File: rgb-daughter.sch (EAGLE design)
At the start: 11 parts, among them J1 INPUT

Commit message: feat(planck): add caps
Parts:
- added C10, C11, C12, C13, C15, C16, C17, C18, C19, C2, C20, C21, C22, C23, C24, C25, C26, C27, C28, C29, C3, C30, C31, C32, C33, C34, C35, C36, C37, C38, C39, C4, C40, C41, C42, C43, C44, C45, C46, C47, C48, C5, C6, C7, C8, C9: 0.1uF, SparkFun-Capacitors:0.1UF-0603-25V-(+80/-20%)
- added FRAME2: FRAME-LETTER, SparkFun-Aesthetics:FRAME-LETTER
- added LED10, LED11, LED12, LED13, LED14, LED15, LED16, LED17, LED18, LED19, LED20, LED21, LED22, LED23, LED24, LED25, LED26, LED27, LED28, LED29, LED30, LED31, LED32, LED33, LED34, LED35, LED36, LED37, LED38, LED39, LED40, LED41, LED42, LED43, LED44, LED45, LED46, LED47, LED7, LED8, LED9: WS2812B5050, adafruit:WS2812B5050
- C1: value 100uF -> 0.1uF; device capacitor-wima:C2,5-3 -> SparkFun-Capacitors:0.1UF-0603-25V-(+80/-20%)
- J1: device SparkFun-Connectors:CONN_05 -> SparkFun-Connectors:CONN_051.27MM
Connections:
- new net DO: LED23.DO, LED25.DI
- new net N$10: LED8.DO, LED9.DI
- new net N$11: LED10.DI, LED9.DO
- new net N$12: LED10.DO, LED11.DI
- new net N$13: LED11.DO, LED12.DI
- new net N$14: LED14.DO, LED15.DI
- new net N$15: LED15.DO, LED16.DI
- new net N$16: LED16.DO, LED17.DI
- new net N$17: LED17.DO, LED18.DI
- new net N$18: LED19.DO, LED20.DI
- new net N$19: LED20.DO, LED21.DI
- new net N$20: LED21.DO, LED22.DI
- new net N$21: LED22.DO, LED23.DI
- new net N$22: LED24.DI, LED47.DO
- new net N$23: LED6.DO, LED7.DI
- new net N$24: LED13.DO, LED14.DI
- new net N$25: LED18.DO, LED19.DI
- new net N$26: LED25.DO, LED26.DI
- new net N$29: LED26.DO, LED27.DI
- new net N$30: LED27.DO, LED28.DI
- new net N$31: LED28.DO, LED29.DI
- new net N$32: LED29.DO, LED30.DI
- new net N$33: LED31.DO, LED32.DI
- new net N$34: LED32.DO, LED33.DI
- new net N$35: LED33.DO, LED34.DI
- new net N$36: LED34.DO, LED35.DI
- new net N$37: LED35.DO, LED36.DI
- new net N$38: LED38.DO, LED39.DI
- new net N$39: LED39.DO, LED40.DI
- new net N$40: LED40.DO, LED41.DI
- new net N$41: LED41.DO, LED42.DI
- new net N$42: LED43.DO, LED44.DI
- new net N$43: LED45.DO, LED46.DI
- new net N$44: LED46.DO, LED47.DI
- new net N$46: LED30.DO, LED31.DI
- new net N$47: LED36.DO, LED37.DI
- new net N$48: LED37.DO, LED38.DI
- new net N$49: LED42.DO, LED43.DI
- new net N$50: LED44.DO, LED45.DI
- new net N$8: LED7.DO, LED8.DI
- new net N$9: LED12.DO, LED13.DI
- net GND: now also C10.2, C11.2, C12.2, C13.2, C15.2, C16.2, C17.2, C18.2, C19.2, C2.2, C20.2, C21.2, C22.2, C23.2, C24.2, C25.2, C26.2, C27.2, C28.2, C29.2, C3.2, C30.2, C31.2, C32.2, C33.2, C34.2, C35.2, C36.2, C37.2, C38.2, C39.2, C4.2, C40.2, C41.2, C42.2, C43.2, C44.2, C45.2, C46.2, C47.2, C48.2, C5.2, C6.2, C7.2, C8.2, C9.2, LED10.GND, LED11.GND, LED12.GND, LED13.GND, LED14.GND, LED15.GND, LED16.GND, LED17.GND, LED18.GND, LED19.GND, LED20.GND, LED21.GND, LED22.GND, LED23.GND, LED24.GND, LED25.GND, LED26.GND, LED27.GND, LED28.GND, LED29.GND, LED30.GND, LED31.GND, LED32.GND, LED33.GND, LED34.GND, LED35.GND, LED36.GND, LED37.GND, LED38.GND, LED39.GND, LED40.GND, LED41.GND, LED42.GND, LED43.GND, LED44.GND, LED45.GND, LED46.GND, LED47.GND, LED7.GND, LED8.GND, LED9.GND
- net VDD: now also C10.1, C11.1, C12.1, C13.1, C15.1, C16.1, C17.1, C18.1, C19.1, C2.1, C20.1, C21.1, C22.1, C23.1, C24.1, C25.1, C26.1, C27.1, C28.1, C29.1, C3.1, C30.1, C31.1, C32.1, C33.1, C34.1, C35.1, C36.1, C37.1, C38.1, C39.1, C4.1, C40.1, C41.1, C42.1, C43.1, C44.1, C45.1, C46.1, C47.1, C48.1, C5.1, C6.1, C7.1, C8.1, C9.1, LED10.VDD, LED11.VDD, LED12.VDD, LED13.VDD, LED14.VDD, LED15.VDD, LED16.VDD, LED17.VDD, LED18.VDD, LED19.VDD, LED20.VDD, LED21.VDD, LED22.VDD, LED23.VDD, LED24.VDD, LED25.VDD, LED26.VDD, LED27.VDD, LED28.VDD, LED29.VDD, LED30.VDD, LED31.VDD, LED32.VDD, LED33.VDD, LED34.VDD, LED35.VDD, LED36.VDD, LED37.VDD, LED38.VDD, LED39.VDD, LED40.VDD, LED41.VDD, LED42.VDD, LED43.VDD, LED44.VDD, LED45.VDD, LED46.VDD, LED47.VDD, LED7.VDD, LED8.VDD, LED9.VDD

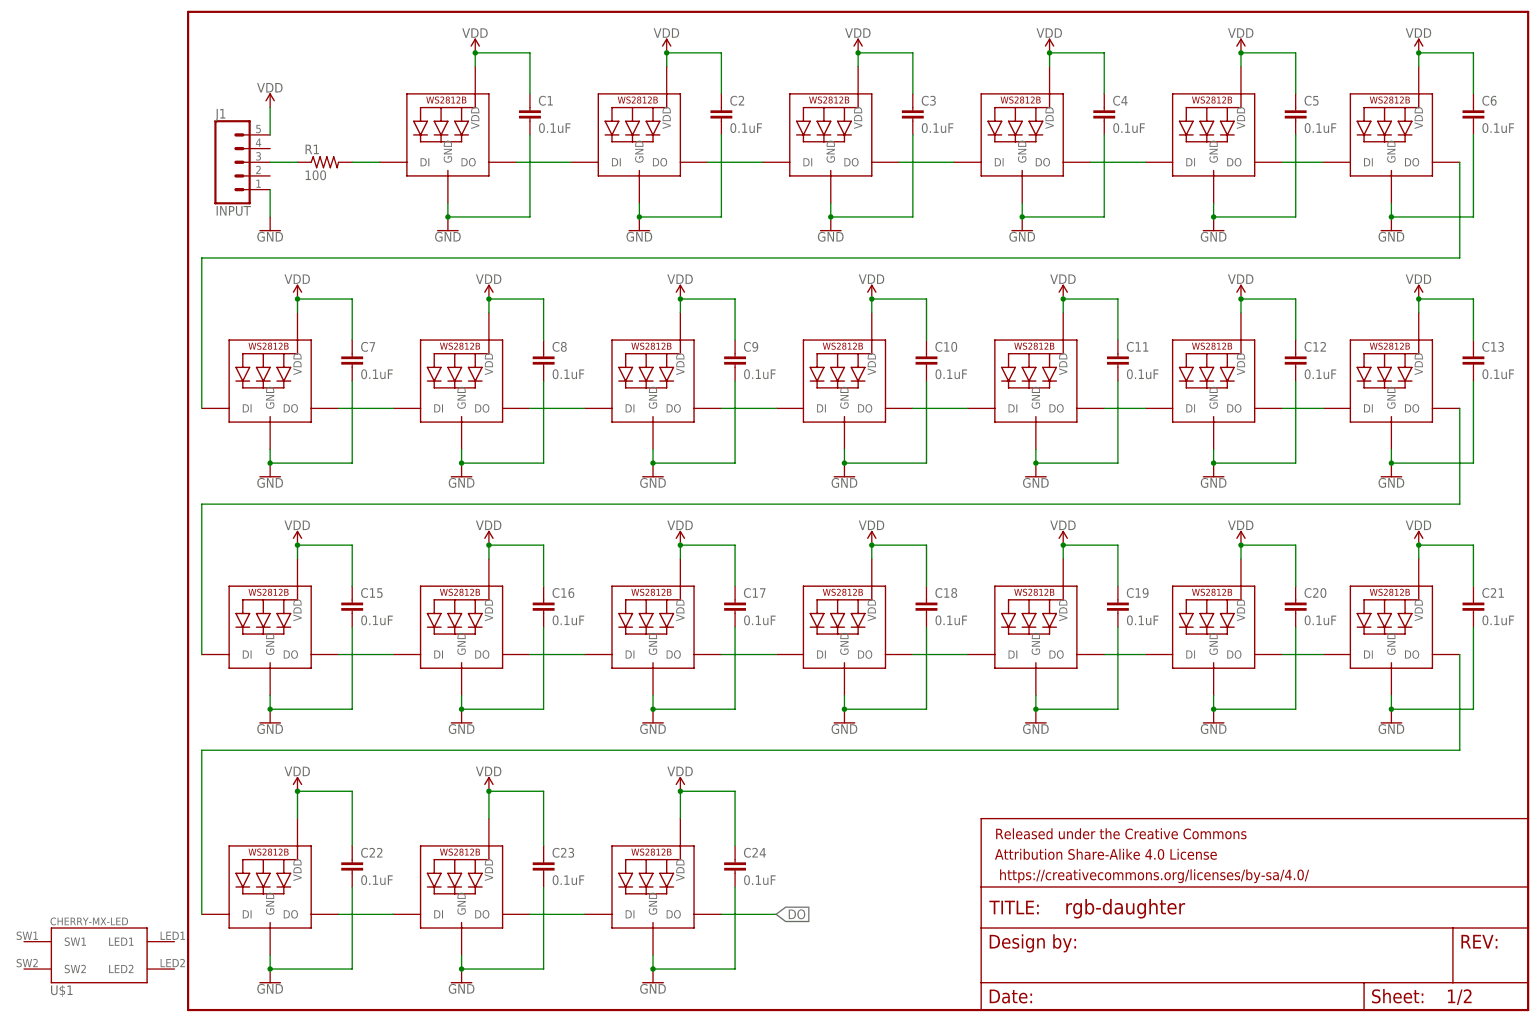
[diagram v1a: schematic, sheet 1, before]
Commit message: 🐛 rebuilding schematic with design blocks
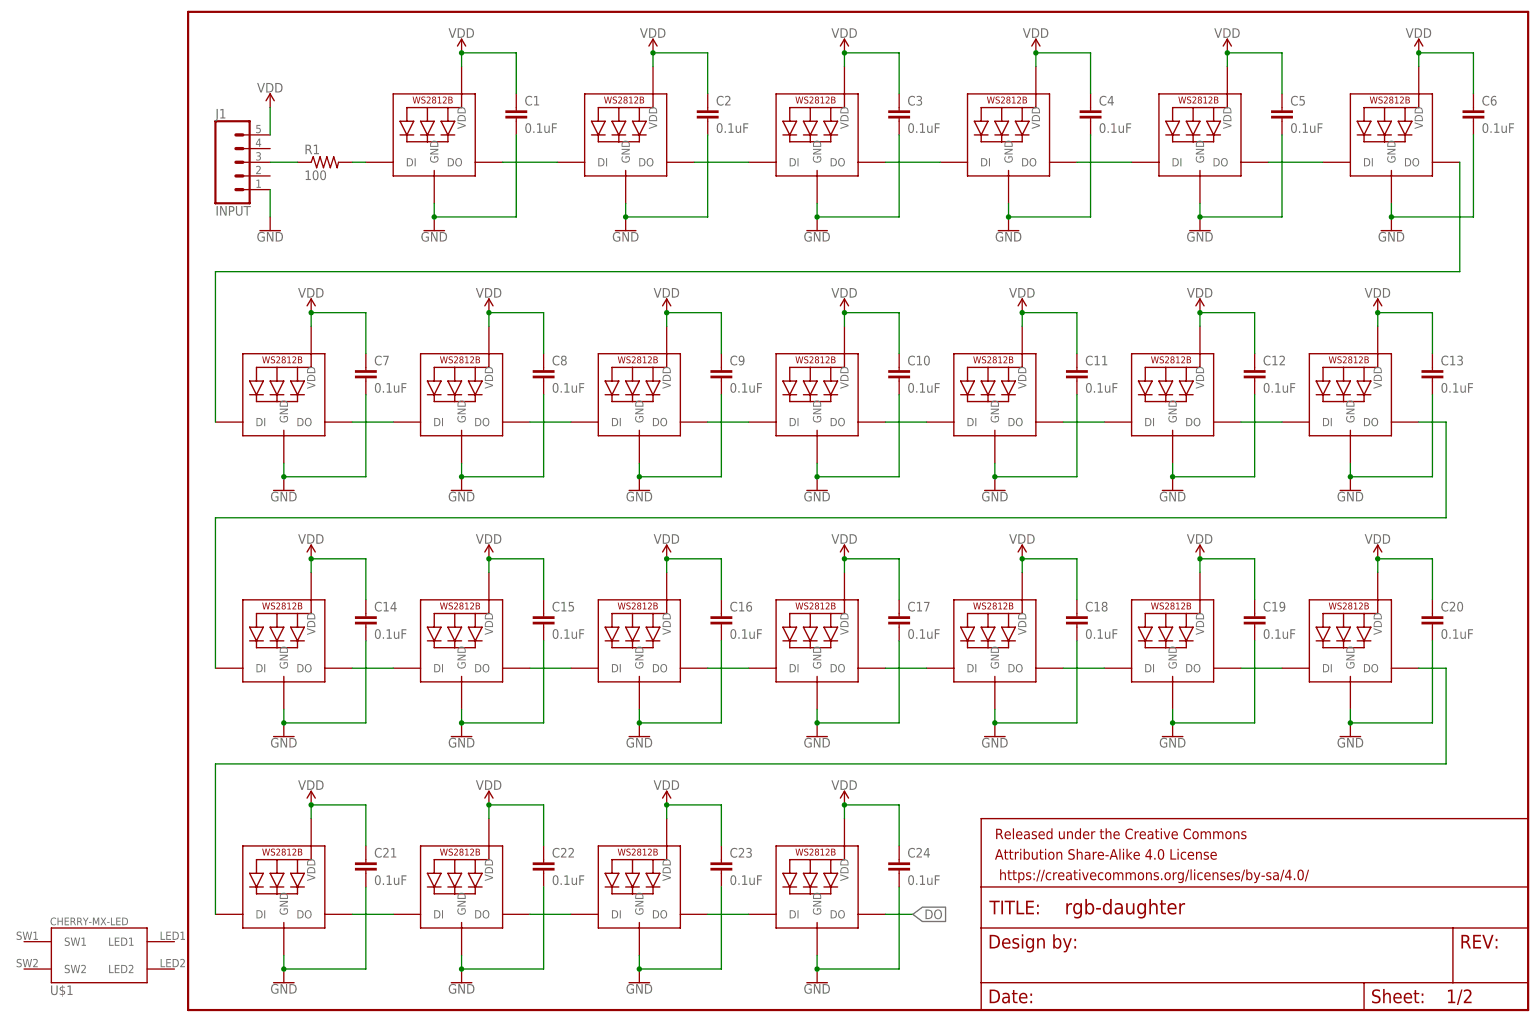
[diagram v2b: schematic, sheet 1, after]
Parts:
- added C14: 0.1uF, SparkFun-Capacitors:0.1UF-0603-25V-(+80/-20%)
- added LED48: WS2812B5050, adafruit:WS2812B5050
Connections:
- new net N$25: LED23.DO, LED48.DI
- net DO: now also LED24.DI, LED48.DO; no longer LED23.DO, LED25.DI
- net GND: now also C14.2, LED48.GND
- net N$22: now also LED24.DO, LED25.DI; no longer LED24.DI, LED47.DO
- net VDD: now also C14.1, LED48.VDD
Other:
- moved on the sheet: C1, C10, C11, C12, C13, C15, C16, C17, C18, C19, C2, C20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

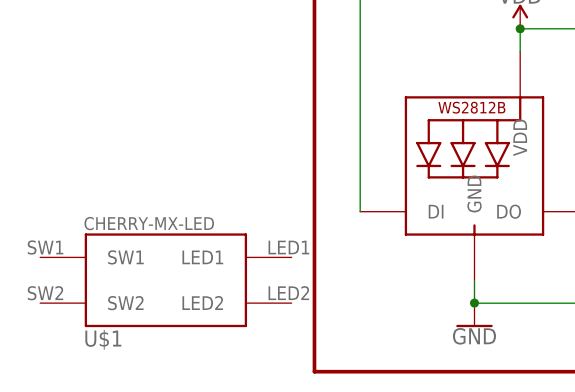
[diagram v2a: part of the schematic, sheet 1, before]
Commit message: 🔥 removing test cherry switch
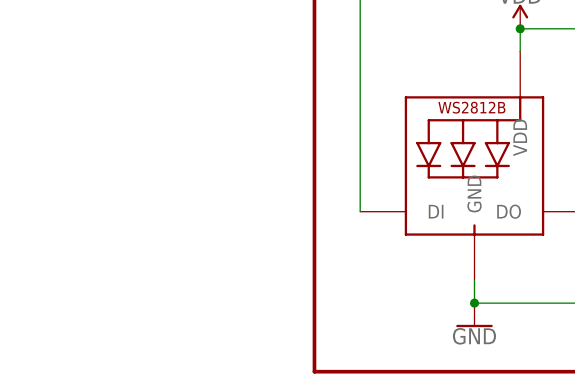
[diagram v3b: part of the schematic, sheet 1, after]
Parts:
- removed U$1: CHERRY-MX-LED, cherrymx:CHERRY-MX-LED
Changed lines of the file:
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@@
 <part name="SUPPLY1" library="SparkFun-PowerSymbols" library_urn="urn:adsk.eagle:library:530" deviceset="VDD" device=""/>
 <part name="R1" library="resistor" library_urn="urn:adsk.eagle:library:348" deviceset="R-US_" device="M0805" package3d_urn="urn:adsk.eagle:package:26079/1" value="100"/>
-<part name="U$1" library="cherrymx" deviceset="CHERRY-MX-LED" device=""/>
 <part name="FRAME2" library="SparkFun-Aesthetics" library_urn="urn:adsk.eagle:library:507" deviceset="FRAME-LETTER" device="" package3d_urn="urn:adsk.eagle:package:37121/1"/>
 <part name="LED1" library="adafruit" library_urn="urn:adsk.eagle:library:420" deviceset="WS2812B" device="5050"/>
@@
 <instance part="SUPPLY1" gate="VDD" x="15.24" y="167.64"/>
 <instance part="R1" gate="G$1" x="25.4" y="157.48"/>
-<instance part="U$1" gate="G$1" x="-20.32" y="10.16"/>
 <instance part="LED1" gate="G$1" x="45.72" y="160.02"/>
 <instance part="C1" gate="G$1" x="60.96" y="165.1"/>

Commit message: ⏪ Revert "🔥 removing test cherry switch"
This reverts commit f0bcf8e92973c98fa4b33c8b3d8bb0c59f9eaaca.
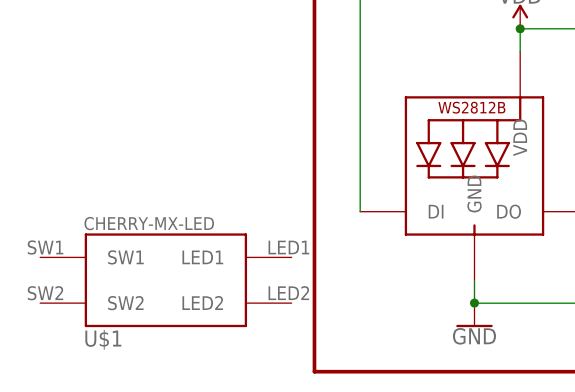
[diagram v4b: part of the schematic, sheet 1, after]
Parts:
- added U$1: CHERRY-MX-LED, cherrymx:CHERRY-MX-LED
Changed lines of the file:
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@@
 <part name="SUPPLY1" library="SparkFun-PowerSymbols" library_urn="urn:adsk.eagle:library:530" deviceset="VDD" device=""/>
 <part name="R1" library="resistor" library_urn="urn:adsk.eagle:library:348" deviceset="R-US_" device="M0805" package3d_urn="urn:adsk.eagle:package:26079/1" value="100"/>
+<part name="U$1" library="cherrymx" deviceset="CHERRY-MX-LED" device=""/>
 <part name="FRAME2" library="SparkFun-Aesthetics" library_urn="urn:adsk.eagle:library:507" deviceset="FRAME-LETTER" device="" package3d_urn="urn:adsk.eagle:package:37121/1"/>
 <part name="LED1" library="adafruit" library_urn="urn:adsk.eagle:library:420" deviceset="WS2812B" device="5050"/>
@@
 <instance part="SUPPLY1" gate="VDD" x="15.24" y="167.64"/>
 <instance part="R1" gate="G$1" x="25.4" y="157.48"/>
+<instance part="U$1" gate="G$1" x="-20.32" y="10.16"/>
 <instance part="LED1" gate="G$1" x="45.72" y="160.02"/>
 <instance part="C1" gate="G$1" x="60.96" y="165.1"/>

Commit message: 🚧📦 using ws2812b 3535
routes are currently screwed up
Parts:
- LED1, LED10, LED11, LED12, LED13, LED14, LED15, LED16, LED17, LED18, LED19, LED2, LED20, LED21, LED22, LED23, LED24, LED25, LED26, LED27, LED28, LED29, LED3, LED30, LED31, LED32, LED33, LED34, LED35, LED36, LED37, LED38, LED39, LED4, LED40, LED41, LED42, LED43, LED44, LED45, LED46, LED47, LED48, LED5, LED6, LED7, LED8, LED9: value WS2812B5050 -> WS2812B3535; device adafruit:WS2812B5050 -> adafruit:WS2812B3535

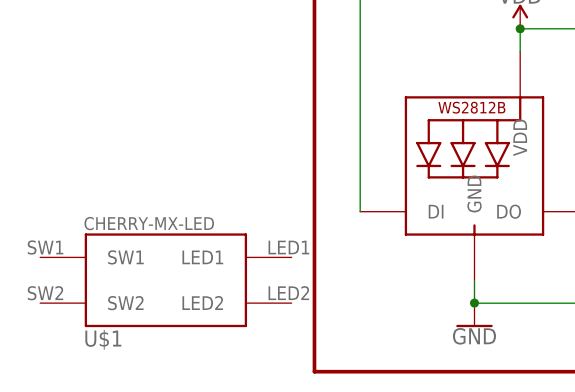
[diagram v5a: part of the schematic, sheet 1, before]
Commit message: 🔥 removing test cherry switch
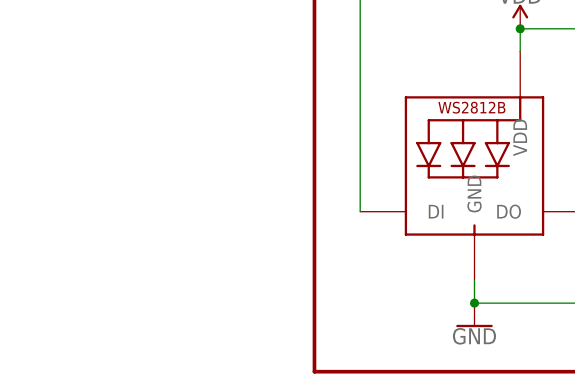
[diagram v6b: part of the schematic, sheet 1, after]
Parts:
- removed U$1: CHERRY-MX-LED, cherrymx:CHERRY-MX-LED
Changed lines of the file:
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@@
 <part name="SUPPLY1" library="SparkFun-PowerSymbols" library_urn="urn:adsk.eagle:library:530" deviceset="VDD" device=""/>
 <part name="R1" library="resistor" library_urn="urn:adsk.eagle:library:348" deviceset="R-US_" device="M0805" package3d_urn="urn:adsk.eagle:package:26079/1" value="100"/>
-<part name="U$1" library="cherrymx" deviceset="CHERRY-MX-LED" device=""/>
 <part name="FRAME2" library="SparkFun-Aesthetics" library_urn="urn:adsk.eagle:library:507" deviceset="FRAME-LETTER" device="" package3d_urn="urn:adsk.eagle:package:37121/1"/>
 <part name="LED1" library="adafruit" library_urn="urn:adsk.eagle:library:420" deviceset="WS2812B" device="3535" value="WS2812B3535"/>
@@
 <instance part="SUPPLY1" gate="VDD" x="15.24" y="167.64"/>
 <instance part="R1" gate="G$1" x="25.4" y="157.48"/>
-<instance part="U$1" gate="G$1" x="-20.32" y="10.16"/>
 <instance part="LED1" gate="G$1" x="45.72" y="160.02"/>
 <instance part="C1" gate="G$1" x="60.96" y="165.1"/>

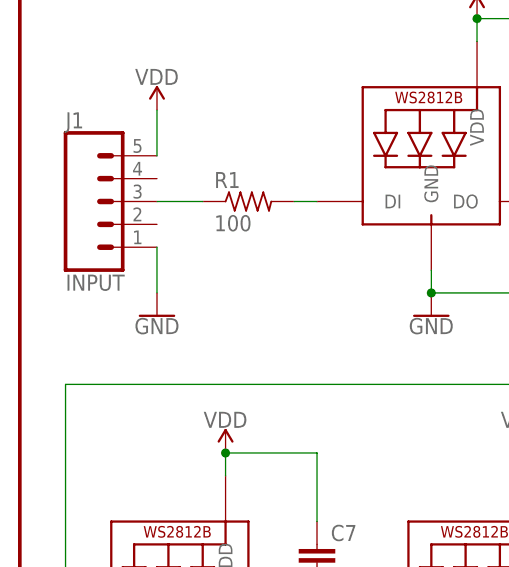
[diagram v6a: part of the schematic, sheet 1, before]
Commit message: 💄 converting text labels to attributes
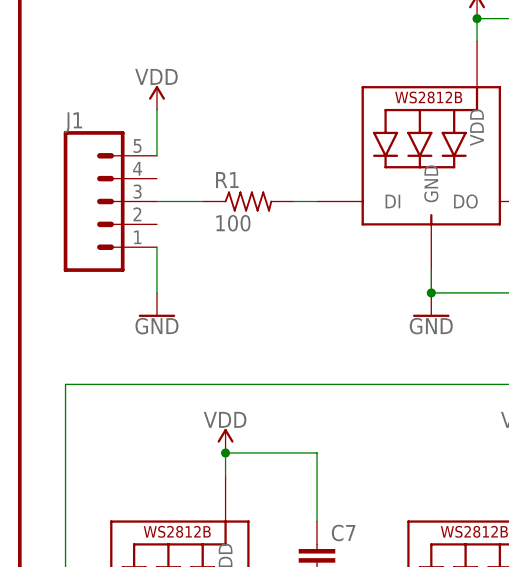
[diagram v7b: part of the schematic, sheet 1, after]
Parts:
- J1: value INPUT -> (none)
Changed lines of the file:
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@@
 <part name="FRAME1" library="SparkFun-Aesthetics" library_urn="urn:adsk.eagle:library:507" deviceset="FRAME-LETTER" device="" package3d_urn="urn:adsk.eagle:package:37121/1"/>
 <part name="GND1" library="SparkFun-PowerSymbols" library_urn="urn:adsk.eagle:library:530" deviceset="GND" device=""/>
-<part name="J1" library="SparkFun-Connectors" library_urn="urn:adsk.eagle:library:513" deviceset="CONN_05" device="1.27MM" package3d_urn="urn:adsk.eagle:package:38110/1" value="INPUT"/>
+<part name="J1" library="SparkFun-Connectors" library_urn="urn:adsk.eagle:library:513" deviceset="CONN_05" device="1.27MM" package3d_urn="urn:adsk.eagle:package:38110/1"/>
 <part name="SUPPLY1" library="SparkFun-PowerSymbols" library_urn="urn:adsk.eagle:library:530" deviceset="VDD" device=""/>
 <part name="R1" library="resistor" library_urn="urn:adsk.eagle:library:348" deviceset="R-US_" device="M0805" package3d_urn="urn:adsk.eagle:package:26079/1" value="100"/>

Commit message: 🚧✨ create USB Type-C part
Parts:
- added FRAME3: FRAME-LETTER, SparkFun-Aesthetics:FRAME-LETTER
- added U$1: USB-TYPE-CDX07S024JJ3R1300, usb:USB-TYPE-CDX07S024JJ3R1300
- added USB-HEADER: (no value), SparkFun-Connectors:CONN_041.27MM
- renumbered J1 to EXTENSION
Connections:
- new net USB-D+: U$1.A6, U$1.B6, USB-HEADER.2
- new net USB-D-: U$1.A7, U$1.B7, USB-HEADER.3
- net GND: now also U$1.A1, U$1.A12, U$1.B1, U$1.B12, USB-HEADER.1
- net VDD: now also U$1.A4, U$1.A9, U$1.B4, U$1.B9, USB-HEADER.4
